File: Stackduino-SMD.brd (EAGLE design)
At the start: 62.5 x 75 mm, 47 parts

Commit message: Latest progress
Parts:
- added C13: 22uF, eagle-ltspice:C0805
- added R6: 10K, eagle-ltspice:R0805
- MP1: value (none) -> FDN306P
- moved R2 1.74 mm to (14.9, 59.6)
- moved C9 0.53 mm to (55.0, 33.2)
- moved R21 0.51 mm to (46.5, 67.1)
- moved C6 0.25 mm to (11.4, 42.4)
- moved R5 0.05 mm to (41.5, 24.2)
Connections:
- net GND: now also C13.2
- net KILL: now also R6.1
- net V+: now also C13.1
- net VCC: now also R6.2
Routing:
- net VCC: track 243.8 -> 272.8 mm
- net V+: track 163.5 -> 169.1 mm
- net KILL: track 47.5 -> 51.5 mm
- net N$44: track 8.07 -> 9.07 mm
- net DIG1: track 65.0 -> 66.0 mm
- net ALOG2: track 41.8 -> 42.7 mm
- net N$1: track 25.9 -> 26.5 mm
- net N$21: track 35.0 -> 34.4 mm
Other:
- board text added: "A4988 Carrier"

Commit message: latest progress
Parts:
- removed R18, R19: 4.7K, eagle-ltspice:R0805
- removed R22: 470K, eagle-ltspice:R0805
- added R10: 1.5K, eagle-ltspice:R0805
- added R7: 220K, eagle-ltspice:R0805
- C1: value 10nF -> 22uF
- C10: value 0.1uF -> 100nF
- C11: value 0.1uF -> (none)
- C13: value 22uF -> 0.1uF
- C2: value (none) -> 100uF; device eagle-ltspice:C0805 -> SparkFun-Passives:PANASONIC_D
- C3: value 100uF -> 10nF; device SparkFun-Passives:PANASONIC_D -> eagle-ltspice:C0805
- C4: value 0.1uF -> 68uF; device eagle-ltspice:C0805 -> SparkFun-Passives:PANASONIC_D
- C6: value 68uF -> 100uF
- C7: value 100nF -> 0.1uF
- C9: value 100uF -> 0.1uF; device SparkFun-Passives:PANASONIC_D -> eagle-ltspice:C0805
- R1: value 1.5K -> 470K
- R3, R4: value 220K -> 4.7K
- R6: value 10K -> 220K
- moved C4 46.5 mm to (11.4, 42.4), turned to 180 degrees
- moved C6 44.6 mm to (55.0, 33.2)
- moved D1 42.6 mm to (3.18, 69.0), turned to 0 degrees
- moved D2 42.6 mm to (2.29, 26.4), turned to 90 degrees
- moved C8 36.9 mm to (57.8, 45.7)
- moved C2 34.2 mm to (4.45, 47.0), turned to 0 degrees
- moved C1 32.9 mm to (6.99, 65.0), turned to 90 degrees
- moved C7 32.2 mm to (51.7, 38.3), turned to 0 degrees
- moved R6 29.6 mm to (47.2, 54.8)
- moved C9 27.6 mm to (55.6, 60.7)
- moved R4 26.7 mm to (28.2, 38.8), turned to 90 degrees
- moved C11 26.6 mm to (44.5, 55.6), turned to 0 degrees
- moved R3 26.3 mm to (26.3, 38.8), turned to 270 degrees
- moved R1 23.6 mm to (17.7, 66.2)
- moved C5 19.5 mm to (33.1, 32.5), turned to 180 degrees
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- renumbered R20 to R9, R21 to R8
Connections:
- net GND: now also C1.2, C10.2, C11.2, C2.-, C4.-, C5.1, C9.1, D2.A; no longer C10.1, C11.1, C2.2, C3.-, C5.2, C8.2, C9.-, D1.A
- net KILL: no longer R6.1
- net N$11: now also C8.1, R10.1; no longer C4.1, R1.1
- net N$15: now also C12.1; no longer C2.1
- net N$16: now also C11.1; no longer C12.1
- net N$18: now also R4.1; no longer R19.1
- net N$19: now also R3.2; no longer R18.2
- net N$3: now also C8.2; no longer C4.2
- net N$31: now also R6.2; no longer R3.2
- net N$32: now also R7.2; no longer R4.2
- net N$34: now also R6.1; no longer R3.1
- net N$36: now also R7.1; no longer R4.1
- net N$4: now also C3.1; no longer C1.1
- net N$43: now also C10.1; no longer C7.1
- net N$7: now also C3.2, D2.C; no longer C1.2, D1.C
- net STAT: now also R1.1; no longer R22.1
- net V+: now also C1.1, C2.+, C6.+, D1.C; no longer C13.1, C3.+, C9.+, D2.C
- net VCC: now also C13.1, C4.+, C5.2, C7.1, C9.2, R10.2, R3.1, R4.2; no longer C10.2, C11.2, C5.1, C6.+, C8.1, R18.1, R19.2, R22.2, R6.2
- net VIN: now also D1.A; no longer D2.A
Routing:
- net VCC: track 272.8 -> 304.0 mm
- net DIG2: track 138.5 -> 125.4 mm
- net KILL: track 51.5 -> 47.5 mm
- net INT: track 44.0 -> 40.1 mm
- net GND: track 51.1 -> 48.0 mm
- net N$28: track 54.0 -> 56.9 mm
- net V+: track 169.1 -> 166.9 mm
- net DIG1: track 66.0 -> 67.5 mm
- net VIN: track 8.32 -> 9.27 mm

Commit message: latest progress
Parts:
- removed ROTARY_ENCODER: ROTARTY_ENCODER, SparkFun-Electromechanical:ROTARY_ENC_PLAIN
- removed S1: (no value), adafruit:B3F-31XX
- removed S2: (no value), adafruit:B3F-40XX-ROUND
- removed S3: Forward, SparkFun-Electromechanical:TACTILE-PTH
- removed S4: Backward, SparkFun-Electromechanical:TACTILE-PTH
- added ENCODER: JST-PH_3-PIN_HEADER, SRG:JST_B3B-PH_HEADER
- added FWD/BWD: JST-PH_4-PIN_HEADER, SRG:JST_B4B-PH_HEADER
- added MENU_SEL, ON/OFF, START/STOP: JST-PH_2-PIN_HEADER, SRG:JST_B2B-PH_HEADER
- BATT: device adafruit:JST-PH-2-THM -> adafruit:JST-PH-2-THM-RA
- moved R5 9.45 mm to (50.3, 27.5), turned to 90 degrees
- moved BATT 6.69 mm to (10.7, 55.6), turned to 90 degrees
- moved D1 2.13 mm to (2.62, 66.9), turned to 270 degrees
- moved C1 1.83 mm to (8.00, 66.5), turned to 180 degrees
- moved C7 0.38 mm to (51.3, 38.3)
- moved R2 0.30 mm to (15.2, 59.6)
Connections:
- net N$15 renamed XTAL2
- net N$16 renamed XTAL1
- net N$31 renamed PD6
- net N$32 renamed PD7
- removed net N$20: ATMEGA328P.23, ROTARY_ENCODER.A
- removed net N$21: ATMEGA328P.24, ROTARY_ENCODER.B
- new net PC0: ATMEGA328P.23, ENCODER.P1
- new net PC1: ATMEGA328P.24, ENCODER.P3
- net ENCSWITCH: now also MENU_SEL.P2; no longer ROTARY_ENCODER.SW-
- net GND: now also ENCODER.P2, FWD/BWD.P1, FWD/BWD.P3, MENU_SEL.P1, ON/OFF.P2, START/STOP.P1; no longer ROTARY_ENCODER.C, ROTARY_ENCODER.SW+, S1.1, S2.2, S3.2, S4.2
- net MISO: now also ATMEGA328P.16; no longer ATMEGA328P.15
- net MOSI: now also ATMEGA328P.15; no longer ATMEGA328P.16
- net N$28: now also START/STOP.P2; no longer S2.4
- net N$33: now also FWD/BWD.P2; no longer S4.4
- net N$35: now also FWD/BWD.P4; no longer S3.4
- net N$8: now also ON/OFF.P1; no longer S1.2
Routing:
- net PC0: track 0.00 -> 51.8 mm, vias 0 -> 1
- net PC1: track 0.00 -> 45.4 mm, vias 0 -> 1
- net N$20: track 43.3 -> 0.00 mm, vias 1 -> 0
- net N$8: track 6.88 -> 45.0 mm, vias 0 -> 1
- net N$21: track 34.4 -> 0.00 mm, vias 1 -> 0
- net N$33: track 29.3 -> 12.2 mm
- net VCC: track 304.0 -> 291.8 mm
- net N$28: track 56.9 -> 45.1 mm
- net N$2: track 2.63 -> 11.4 mm
- net ENCSWITCH: track 24.1 -> 18.0 mm
- net MISO: track 38.9 -> 43.9 mm
- net N$35: track 16.8 -> 12.5 mm
- net MOSI: track 43.9 -> 39.9 mm
- net V+: track 166.9 -> 169.9 mm
- net VDD: track 27.2 -> 24.6 mm
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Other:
- board size 62.5 x 75 mm -> 62.7 x 64.1 mm
- board text added: "B"
- board text added: "D"
- board text added: "E"
- board text added: "F"
- board text added: "G"

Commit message: Latest progress
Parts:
- moved C1 3.52 mm to (6.48, 63.4)
- moved ENCODER 1.52 mm to (45.8, 22.1)
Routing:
- net VCC: track 291.8 -> 295.2 mm
- net DIG2: track 124.3 -> 121.1 mm
- net PC0: track 51.8 -> 53.4 mm
- net PC1: track 45.4 -> 46.9 mm
- net N$8: track 45.0 -> 43.7 mm
- net V+: track 169.9 -> 169.2 mm
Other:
- board size 62.7 x 64.1 mm -> 62.6 x 64.4 mm

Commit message: Latest progress
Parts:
- moved C5 16.2 mm to (17.2, 35.6)
- moved MP1 1.91 mm to (13.0, 49.8)
- moved C2 1.07 mm to (4.22, 48.0)
- moved C4 1.05 mm to (11.8, 43.4), turned to 270 degrees
- moved R10 0.69 mm to (31.7, 46.4)
- moved L1 0.25 mm to (10.8, 31.9)
- moved C10 0.13 mm to (58.6, 69.7)
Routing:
- net GND: track 47.7 -> 35.7 mm, vias 10 -> 11
- net VDD: track 24.6 -> 20.9 mm
- net N$2: track 11.4 -> 13.7 mm
- net V+: track 169.2 -> 171.5 mm
- net N$10: track 20.9 -> 19.2 mm
- net KILL: track 47.5 -> 45.9 mm
- net N$1: track 26.5 -> 25.4 mm
- net SLEEP: track 17.9 -> 18.8 mm
- net PC0: track 53.4 -> 52.8 mm
- net DIG2: track 121.1 -> 121.6 mm

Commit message: latest progress
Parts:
- moved C5 6.66 mm to (23.4, 38.0), turned to 270 degrees
- moved C1 3.66 mm to (2.97, 62.3), turned to 270 degrees
- moved C3 1.14 mm to (3.31, 31.9)
- moved D1 0.86 mm to (2.97, 67.7)
- moved C2 0.38 mm to (4.22, 48.4)
- moved C6 0.36 mm to (55.4, 33.2)
- moved LTC4412 0.36 mm to (12.3, 65.6)
- moved D2 0.31 mm to (2.37, 26.1)
- moved MP1 0.25 mm to (13.0, 50.1)
- moved R5 0.20 mm to (50.5, 27.5)
- moved C4 0.11 mm to (11.9, 43.5)
- moved FWD/BWD 0.05 mm to (16.6, 22.1)
- moved ENCODER 0.05 mm to (45.8, 22.1)
- moved START/STOP 0.05 mm to (54.1, 22.1)
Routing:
- net V+: track 171.5 -> 141.0 mm, vias 5 -> 8
- net N$7: track 24.4 -> 0.00 mm
- net VIN: track 7.57 -> 0.00 mm
- net VCC: track 295.0 -> 289.6 mm
- net STEP: track 46.2 -> 41.9 mm
- net GND: track 35.7 -> 39.0 mm
- net DIR: track 34.8 -> 32.7 mm
- net OUT2B: track 52.0 -> 53.2 mm
- net VDD: track 20.9 -> 19.7 mm
- net OUT1B: track 48.7 -> 49.6 mm
- net N$4: track 3.03 -> 3.94 mm
- net N$8: track 43.7 -> 43.0 mm
- net N$10: track 19.2 -> 18.6 mm
- net INT: track 40.2 -> 40.8 mm
- added copper zone on layer 1, net N$7
- added copper zone on layer 1, net V+
- added copper zone on layer 1, net VCC
- added copper zone on layer 1, net VIN

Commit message: latest progress
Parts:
- added R0: 470K, eagle-ltspice:R0805
- R1: value 470K -> 100K
- R2: value 10K -> 100K
- moved R1 9.96 mm to (15.2, 56.5), turned to 0 degrees
- moved L1 8.53 mm to (6.98, 24.3), turned to 0 degrees
- moved D2 7.49 mm to (2.44, 33.6), turned to 270 degrees
- moved LM2675 6.60 mm to (8.62, 34.1), turned to 90 degrees
- moved C2 5.67 mm to (3.94, 42.7), turned to 180 degrees
- moved C3 5.60 mm to (8.67, 30.4), turned to 180 degrees
- moved D1 5.18 mm to (3.71, 62.6)
- moved C1 5.17 mm to (3.78, 57.2)
- moved C7 5.08 mm to (51.3, 33.2)
- moved ICSP 5.08 mm to (52.2, 39.5)
- moved OPT1 5.08 mm to (52.7, 51.7)
- moved R3 5.08 mm to (26.3, 33.7)
- moved R4 5.08 mm to (28.2, 33.7)
- moved R8 5.08 mm to (46.5, 62.1)
- moved ENCODER 5.08 mm to (45.8, 17.0)
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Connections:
- net KILL: now also R1.1
- net STAT: now also R0.1; no longer R1.1
- net VCC: now also R0.2
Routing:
- net V+: track 141.0 -> 156.1 mm
- net VCC: track 289.6 -> 294.2 mm
- net N$4: track 3.94 -> 0.00 mm
- net DIG2: track 121.6 -> 118.2 mm, vias 0 -> 2
- net N$5: track 8.40 -> 11.1 mm
- net N$6: track 7.21 -> 9.87 mm
- net KILL: track 46.2 -> 48.6 mm
- net INT: track 40.8 -> 43.0 mm
- net N$44: track 9.07 -> 10.8 mm
- net GND: track 39.0 -> 37.8 mm
- net STAT: track 69.6 -> 70.8 mm
- net N$10: track 18.6 -> 17.4 mm
- net VDD: track 19.7 -> 18.8 mm
- net N$43: track 12.2 -> 11.5 mm
- net N$30: track 11.1 -> 11.7 mm
- added copper zone on layer 1, net N$4
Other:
- board size 62.6 x 64.4 mm -> 62.6 x 66.8 mm

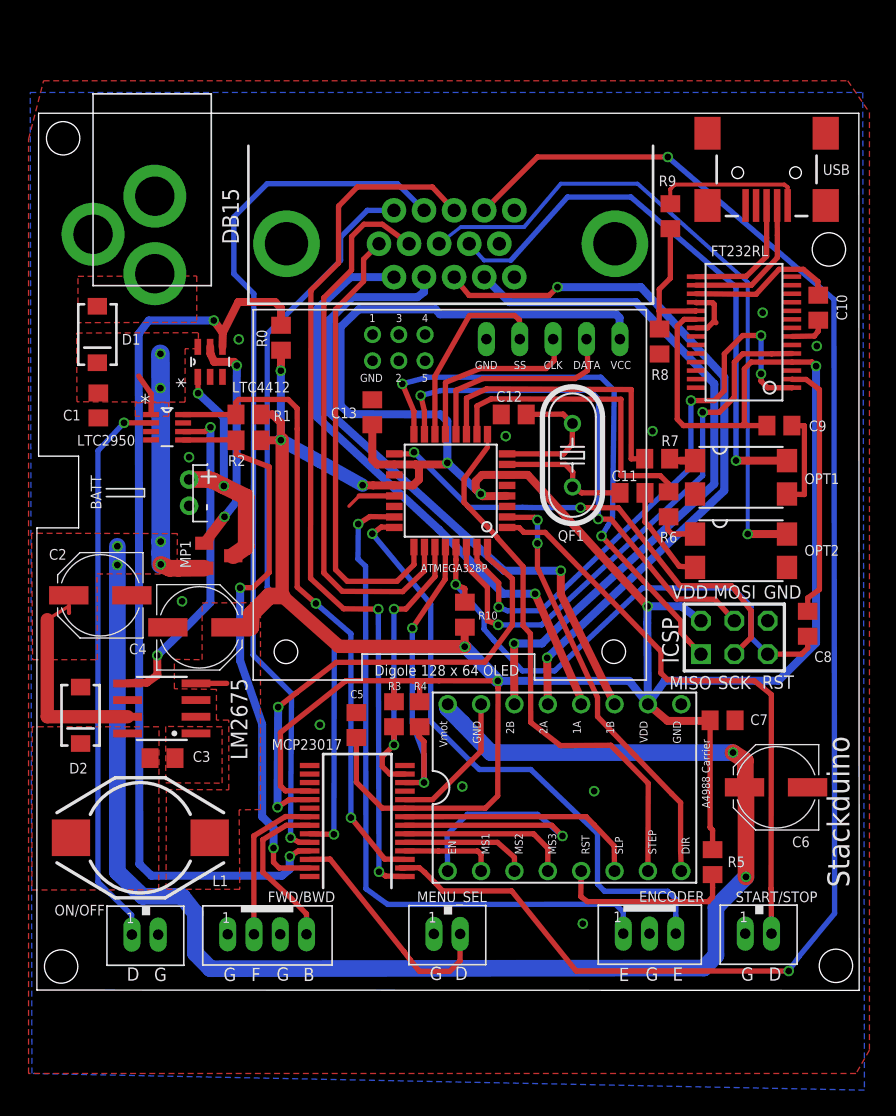
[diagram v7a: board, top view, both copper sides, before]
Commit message: Fixed tx/rx and test pin errors
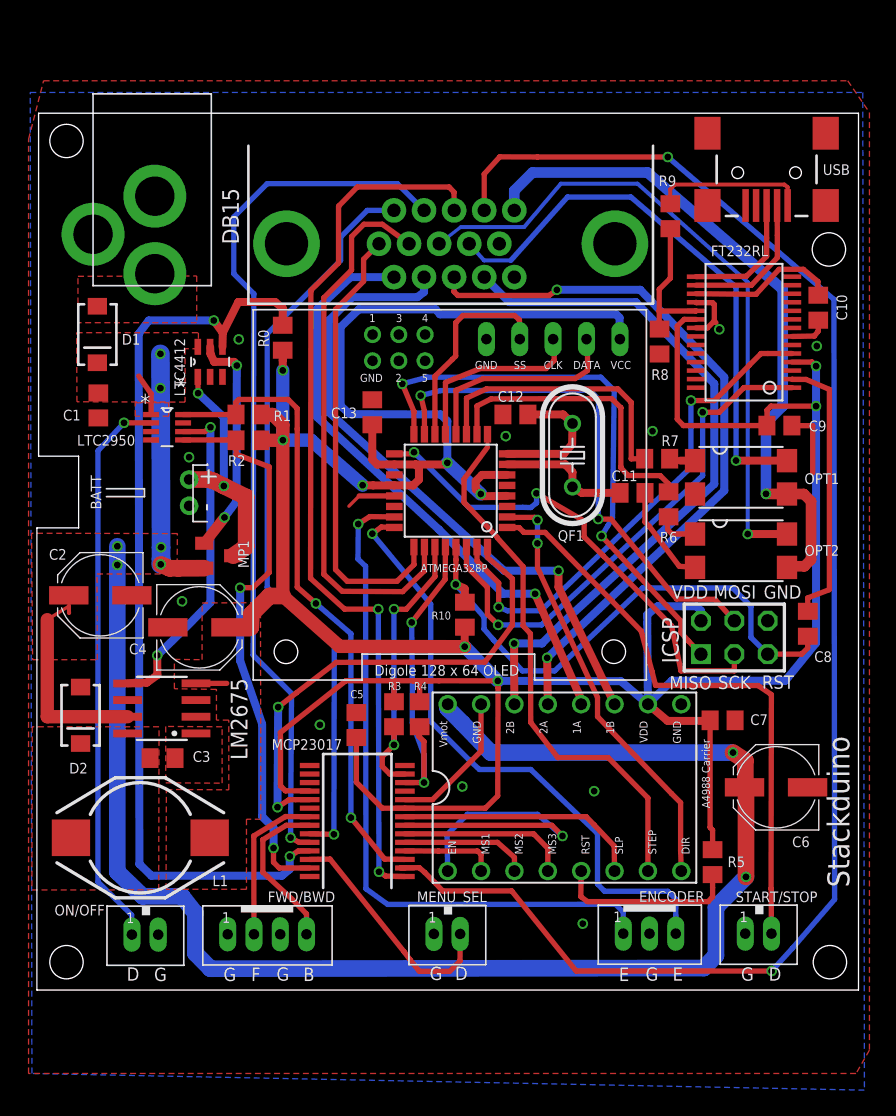
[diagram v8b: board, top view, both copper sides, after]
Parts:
- C11, C12: value (none) -> 0.1uF
- QF1: value (none) -> 16Mhz
- R10: value 1.5K -> 10K
- moved R0 0.13 mm to (17.8, 62.4)
- moved C12 0.13 mm to (35.5, 56.5)
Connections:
- net N$8 renamed PBUTTON
- new net CAM_GND: DB15.15, OPT1.3, OPT2.3
- net GND: now also FT232RL.26; no longer DB15.15, OPT1.3, OPT2.3
- net N$13: now also FT232RL.5; no longer FT232RL.1
- net N$14: now also FT232RL.1; no longer FT232RL.5
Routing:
- net CAM_GND: track 0.00 -> 52.1 mm, vias 0 -> 1
- net VCC: track 294.2 -> 276.2 mm
- net N$13: track 44.5 -> 38.6 mm, vias 4 -> 2
- net GND: track 37.8 -> 34.9 mm
- net N$14: track 42.2 -> 39.4 mm
- net N$3: track 19.7 -> 21.0 mm
- net DIG2: track 118.2 -> 119.2 mm
- net DIG1: track 67.5 -> 68.3 mm
- net PD6: track 23.5 -> 22.8 mm
- net N$22: track 15.1 -> 15.8 mm
- net SCK: track 36.6 -> 37.2 mm
- net PD7: track 21.7 -> 21.2 mm
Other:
- board size 62.6 x 66.8 mm -> 62.5 x 66.7 mm
